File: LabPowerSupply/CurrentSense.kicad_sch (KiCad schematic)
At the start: 7 parts

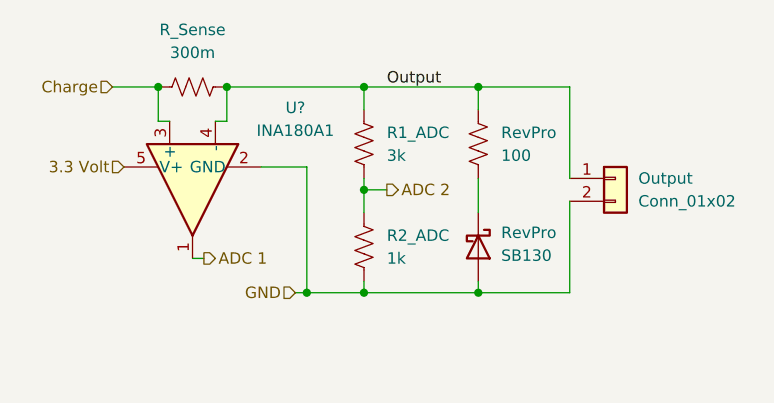
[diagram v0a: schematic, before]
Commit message: Finished first pass on the schematic
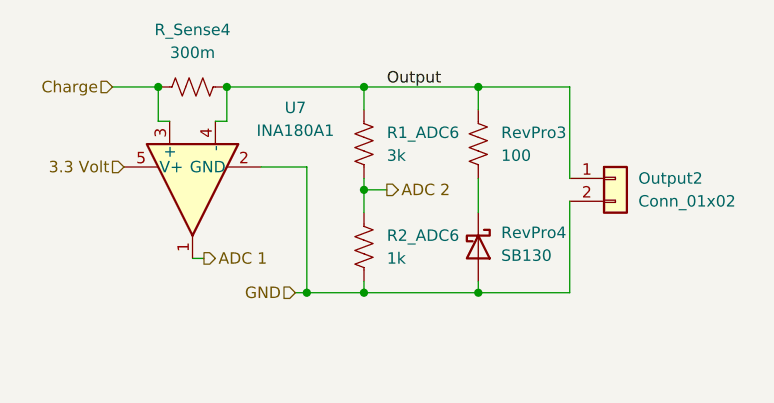
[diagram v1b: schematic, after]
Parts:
- gave numbers to parts that had none: 1
- renumbered Output to Output2, R1_ADC to R1_ADC6, R2_ADC to R2_ADC6, R_Sense to R_Sense4, RevPro to RevPro3, RevPro to RevPro4
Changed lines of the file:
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@@
   (symbol (lib_id "Device:R_US") (at 134.62 83.82 90) (unit 1)
     (in_bom yes) (on_board yes) (fields_autoplaced)
-    (property "Reference" "R_Sense" (id 0) (at 134.62 77.47 90))
+    (property "Reference" "R_Sense4" (id 0) (at 134.62 77.47 90))
     (property "Value" "300m" (id 1) (at 134.62 80.01 90))
     (property "Footprint" "Resistor_SMD:R_1210_3225Metric" (id 2) (at 134.874 82.804 90)
@@
   (symbol (lib_id "Device:R_US") (at 153.67 90.17 0) (unit 1)
     (in_bom yes) (on_board yes) (fields_autoplaced)
-    (property "Reference" "R1_ADC" (id 0) (at 156.21 88.8999 0)
+    (property "Reference" "R1_ADC6" (id 0) (at 156.21 88.8999 0)
       (effects (font (size 1.27 1.27)) (justify left))
     )
@@
   (symbol (lib_id "Device:R_US") (at 166.37 90.17 0) (unit 1)
     (in_bom yes) (on_board yes) (fields_autoplaced)
-    (property "Reference" "RevPro" (id 0) (at 168.91 88.8999 0)
+    (property "Reference" "RevPro3" (id 0) (at 168.91 88.8999 0)
       (effects (font (size 1.27 1.27)) (justify left))
     )
@@
   (symbol (lib_id "Amplifier_Current:INA180A1") (at 134.62 95.25 90) (mirror x) (unit 1)
     (in_bom yes) (on_board yes) (fields_autoplaced)
-    (property "Reference" "U?" (id 0) (at 146.05 86.1312 90))
+    (property "Reference" "U7" (id 0) (at 146.05 86.1312 90))
     (property "Value" "INA180A1" (id 1) (at 146.05 88.6712 90))
     (property "Footprint" "Package_TO_SOT_SMD:SOT-23-5" (id 2) (at 133.35 96.52 0)
@@
   (symbol (lib_id "Connector_Generic:Conn_01x02") (at 181.61 93.98 0) (unit 1)
     (in_bom yes) (on_board yes) (fields_autoplaced)
-    (property "Reference" "Output" (id 0) (at 184.15 93.9799 0)
+    (property "Reference" "Output2" (id 0) (at 184.15 93.9799 0)
       (effects (font (size 1.27 1.27)) (justify left))
     )
@@
   (symbol (lib_id "Diode:SB130") (at 166.37 101.6 270) (unit 1)
     (in_bom yes) (on_board yes) (fields_autoplaced)
-    (property "Reference" "RevPro" (id 0) (at 168.91 100.0124 90)
+    (property "Reference" "RevPro4" (id 0) (at 168.91 100.0124 90)
       (effects (font (size 1.27 1.27)) (justify left))
     )
@@
   (symbol (lib_id "Device:R_US") (at 153.67 101.6 0) (unit 1)
     (in_bom yes) (on_board yes) (fields_autoplaced)
-    (property "Reference" "R2_ADC" (id 0) (at 156.21 100.3299 0)
+    (property "Reference" "R2_ADC6" (id 0) (at 156.21 100.3299 0)
       (effects (font (size 1.27 1.27)) (justify left))
     )

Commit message: started PCB
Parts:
- renumbered U7 to U6
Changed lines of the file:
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@@
   (symbol (lib_id "Amplifier_Current:INA180A1") (at 134.62 95.25 90) (mirror x) (unit 1)
     (in_bom yes) (on_board yes) (fields_autoplaced)
-    (property "Reference" "U7" (id 0) (at 146.05 86.1312 90))
+    (property "Reference" "U6" (id 0) (at 146.05 86.1312 90))
     (property "Value" "INA180A1" (id 1) (at 146.05 88.6712 90))
     (property "Footprint" "Package_TO_SOT_SMD:SOT-23-5" (id 2) (at 133.35 96.52 0)

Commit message: more work
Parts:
- removed RevPro3: 100, Resistor_SMD:R_1210_3225Metric, symbol Device:R_US
- added F_CS1: 320m, Fuse:Fuseholder_Littelfuse_100_series_5x20mm, symbol Device:Fuse
- renumbered U6 to CurrentSense1, RevPro4 to D_CS1, Output2 to Output1, R_Sense4 to R1_CS1, R1_ADC6 to R2_CS1, R2_ADC6 to R3_CS1
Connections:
- net Output: now also D_CS1.1 (K), F_CS1.1; no longer Output1.1 (Pin_1)
- new net: F_CS1.2, Output1.1 (Pin_1)
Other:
- company: (none) -> George Mason University
- title: (none) -> Current and Voltage Sensing
- moved on the sheet: D_CS1
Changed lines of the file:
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@@
 (kicad_sch (version 20211123) (generator eeschema)
   (paper "A4")
+  (title_block
+    (title "Current and Voltage Sensing")
+    (date "2022-09-26")
+    (rev "2")
+    (company "George Mason University")
+    (comment 1 "voltage, and a fuse for reverse polarity protection")
+    (comment 2 "monitered, the voltage senser to both moniter and control the")
+    (comment 3 "user. This stage contains the current senser so that the current can")
+    (comment 4 "This is the final stage before outputting the final voltage for the end")
+  )
   (junction (at 130.81 83.82) (diameter 0) (color 0 0 0 0)
   )
+  (junction (at 153.67 83.82) (diameter 0) (color 0 0 0 0)
+  )
+  (junction (at 153.67 106.68) (diameter 0) (color 0 0 0 0)
+  )
+  (junction (at 153.67 95.25) (diameter 0) (color 0 0 0 0)
+  )
+  (junction (at 147.32 106.68) (diameter 0) (color 0 0 0 0)
+  )
+  (junction (at 138.43 83.82) (diameter 0) (color 0 0 0 0)
+  )
+  (junction (at 166.37 106.68) (diameter 0) (color 0 0 0 0)
+  )
   (junction (at 166.37 83.82) (diameter 0) (color 0 0 0 0)
   )
-  (junction (at 153.67 83.82) (diameter 0) (color 0 0 0 0)
-  )
-  (junction (at 153.67 106.68) (diameter 0) (color 0 0 0 0)
-  )
-  (junction (at 153.67 95.25) (diameter 0) (color 0 0 0 0)
-  )
-  (junction (at 147.32 106.68) (diameter 0) (color 0 0 0 0)
-  )
-  (junction (at 138.43 83.82) (diameter 0) (color 0 0 0 0)
-  )
-  (junction (at 166.37 106.68) (diameter 0) (color 0 0 0 0)
-  )
   (wire (pts (xy 138.43 83.82) (xy 138.43 87.63))
     (stroke (width 0) (type default) (color 0 0 0 0))
@@
     (stroke (width 0) (type default) (color 0 0 0 0))
   )
-  (wire (pts (xy 166.37 93.98) (xy 166.37 97.79))
+  (wire (pts (xy 166.37 83.82) (xy 166.37 91.44))
     (stroke (width 0) (type default) (color 0 0 0 0))
   )
@@
     (stroke (width 0) (type default) (color 0 0 0 0))
   )
+  (wire (pts (xy 175.26 83.82) (xy 176.53 83.82))
+    (stroke (width 0) (type default) (color 0 0 0 0))
+  )
   (wire (pts (xy 153.67 93.98) (xy 153.67 95.25))
     (stroke (width 0) (type default) (color 0 0 0 0))
   )
-  (wire (pts (xy 166.37 83.82) (xy 166.37 86.36))
-    (stroke (width 0) (type default) (color 0 0 0 0))
-  )
   (wire (pts (xy 153.67 95.25) (xy 153.67 97.79))
     (stroke (width 0) (type default) (color 0 0 0 0))
   )
+  (wire (pts (xy 166.37 83.82) (xy 167.64 83.82))
+    (stroke (width 0) (type default) (color 0 0 0 0))
+  )
   (wire (pts (xy 147.32 92.71) (xy 147.32 106.68))
     (stroke (width 0) (type default) (color 0 0 0 0))
@@
     (stroke (width 0) (type default) (color 0 0 0 0))
   )
-  (wire (pts (xy 166.37 105.41) (xy 166.37 106.68))
+  (wire (pts (xy 166.37 99.06) (xy 166.37 106.68))
     (stroke (width 0) (type default) (color 0 0 0 0))
   )
@@
   )
   (wire (pts (xy 146.05 106.68) (xy 147.32 106.68))
-    (stroke (width 0) (type default) (color 0 0 0 0))
-  )
-  (wire (pts (xy 166.37 83.82) (xy 176.53 83.82))
     (stroke (width 0) (type default) (color 0 0 0 0))
   )
@@
     (effects (font (size 1.27 1.27)) (justify right))
   )
+  (symbol (lib_id "Device:Fuse") (at 171.45 83.82 90) (unit 1)
+    (in_bom yes) (on_board yes) (fields_autoplaced)
+    (property "Reference" "F_CS1" (id 0) (at 171.45 77.47 90))
+    (property "Value" "320m" (id 1) (at 171.45 80.01 90))
+    (property "Footprint" "Fuse:Fuseholder_Littelfuse_100_series_5x20mm" (id 2) (at 171.45 85.598 90)
+      (effects (font (size 1.27 1.27)) hide)
+    )
+    (property "Datasheet" "~" (id 3) (at 171.45 83.82 0)
+      (effects (font (size 1.27 1.27)) hide)
+    )
+    (pin "1")
+    (pin "2")
+  )
   (symbol (lib_id "Device:R_US") (at 134.62 83.82 90) (unit 1)
     (in_bom yes) (on_board yes) (fields_autoplaced)
-    (property "Reference" "R_Sense4" (id 0) (at 134.62 77.47 90))
+    (property "Reference" "R1_CS1" (id 0) (at 134.62 77.47 90))
     (property "Value" "300m" (id 1) (at 134.62 80.01 90))
     (property "Footprint" "Resistor_SMD:R_1210_3225Metric" (id 2) (at 134.874 82.804 90)
@@
   (symbol (lib_id "Device:R_US") (at 153.67 90.17 0) (unit 1)
     (in_bom yes) (on_board yes) (fields_autoplaced)
-    (property "Reference" "R1_ADC6" (id 0) (at 156.21 88.8999 0)
+    (property "Reference" "R2_CS1" (id 0) (at 156.21 88.8999 0)
       (effects (font (size 1.27 1.27)) (justify left))
     )
@@
     (pin "2")
   )
-  (symbol (lib_id "Device:R_US") (at 166.37 90.17 0) (unit 1)
-    (in_bom yes) (on_board yes) (fields_autoplaced)
-    (property "Reference" "RevPro3" (id 0) (at 168.91 88.8999 0)
-      (effects (font (size 1.27 1.27)) (justify left))
-    )
-    (property "Value" "100" (id 1) (at 168.91 91.4399 0)
-      (effects (font (size 1.27 1.27)) (justify left))
-    )
-    (property "Footprint" "Resistor_SMD:R_1210_3225Metric" (id 2) (at 167.386 90.424 90)
-      (effects (font (size 1.27 1.27)) hide)
-    )
-    (property "Datasheet" "~" (id 3) (at 166.37 90.17 0)
-      (effects (font (size 1.27 1.27)) hide)
-    )
-    (pin "1")
-    (pin "2")
-  )
   (symbol (lib_id "Amplifier_Current:INA180A1") (at 134.62 95.25 90) (mirror x) (unit 1)
-    (in_bom yes) (on_board yes) (fields_autoplaced)
-    (property "Reference" "U6" (id 0) (at 146.05 86.1312 90))
-    (property "Value" "INA180A1" (id 1) (at 146.05 88.6712 90))
+    (in_bom yes) (on_board yes)
+    (property "Reference" "CurrentSense1" (id 0) (at 124.46 97.79 90))
+    (property "Value" "INA180A1" (id 1) (at 124.46 100.33 90))
     (property "Footprint" "Package_TO_SOT_SMD:SOT-23-5" (id 2) (at 133.35 96.52 0)
       (effects (font (size 1.27 1.27)) hide)
@@
   (symbol (lib_id "Connector_Generic:Conn_01x02") (at 181.61 93.98 0) (unit 1)
     (in_bom yes) (on_board yes) (fields_autoplaced)
-    (property "Reference" "Output2" (id 0) (at 184.15 93.9799 0)
+    (property "Reference" "Output1" (id 0) (at 184.15 93.9799 0)
       (effects (font (size 1.27 1.27)) (justify left))
     )
@@
     (pin "2")
   )
-  (symbol (lib_id "Diode:SB130") (at 166.37 101.6 270) (unit 1)
-    (in_bom yes) (on_board yes) (fields_autoplaced)
-    (property "Reference" "RevPro4" (id 0) (at 168.91 100.0124 90)
-      (effects (font (size 1.27 1.27)) (justify left))
-    )
-    (property "Value" "SB130" (id 1) (at 168.91 102.5524 90)
-      (effects (font (size 1.27 1.27)) (justify left))
-    )
-    (property "Footprint" "Diode_THT:D_DO-41_SOD81_P10.16mm_Horizontal" (id 2) (at 161.925 101.6 0)
-      (effects (font (size 1.27 1.27)) hide)
-    )
-    (property "Datasheet" "http://www.diodes.com/_files/datasheets/ds23022.pdf" (id 3) (at 166.37 101.6 0)
+  (symbol (lib_id "Diode:SB130") (at 166.37 95.25 270) (unit 1)
+    (in_bom yes) (on_board yes) (fields_autoplaced)
+    (property "Reference" "D_CS1" (id 0) (at 168.91 93.6624 90)
+      (effects (font (size 1.27 1.27)) (justify left))
+    )
+    (property "Value" "SB130" (id 1) (at 168.91 96.2024 90)
+      (effects (font (size 1.27 1.27)) (justify left))
+    )
+    (property "Footprint" "Diode_THT:D_DO-41_SOD81_P10.16mm_Horizontal" (id 2) (at 161.925 95.25 0)
+      (effects (font (size 1.27 1.27)) hide)
+    )
+    (property "Datasheet" "http://www.diodes.com/_files/datasheets/ds23022.pdf" (id 3) (at 166.37 95.25 0)
       (effects (font (size 1.27 1.27)) hide)
     )
@@
   (symbol (lib_id "Device:R_US") (at 153.67 101.6 0) (unit 1)
     (in_bom yes) (on_board yes) (fields_autoplaced)
-    (property "Reference" "R2_ADC6" (id 0) (at 156.21 100.3299 0)
-      (effects (font (size 1.27 1.27)) (justify left))
-    )
+    (property "Reference" "R3_CS1" (id 0) (at 156.21 100.3299 0)
+      (effects (font (size 1.27 1.27)) (justify left))
+    )

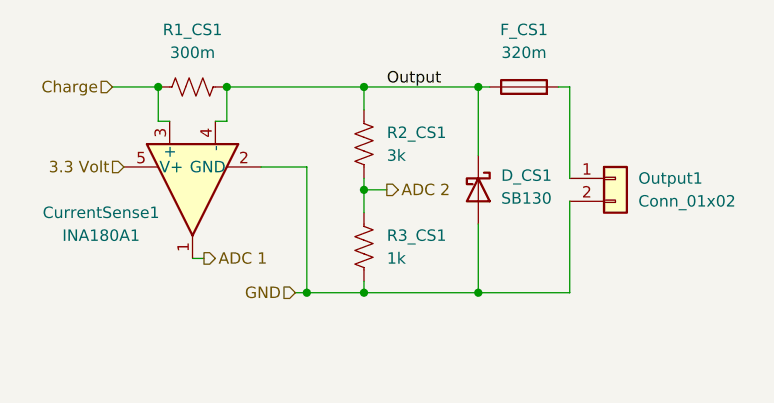
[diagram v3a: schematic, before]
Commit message: Resistor footprints changed to 0603
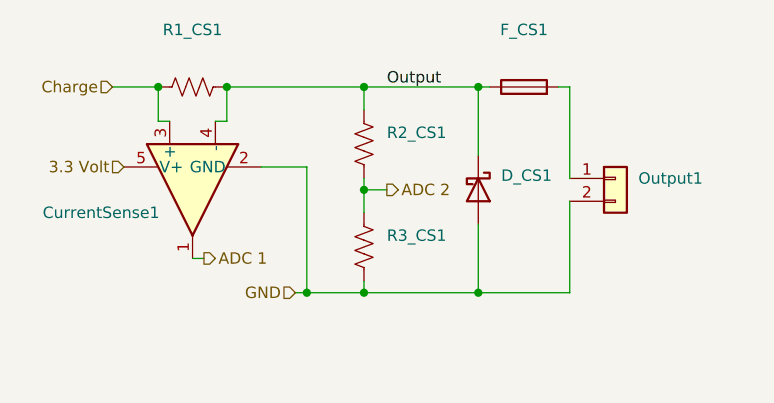
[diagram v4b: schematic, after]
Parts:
- CurrentSense1: value INA180A1 -> (none); footprint Package_TO_SOT_SMD:SOT-23-5 -> (none)
- D_CS1: value SB130 -> (none); footprint Diode_THT:D_DO-41_SOD81_P10.16mm_Horizontal -> (none)
- F_CS1: value 320m -> (none); footprint Fuse:Fuseholder_Littelfuse_100_series_5x20mm -> (none)
- Output1: value Conn_01x02 -> (none); footprint Connector_Wire:SolderWire-2sqmm_1x02_P7.8mm_D2mm_OD3.9mm -> (none)
- R1_CS1: value 300m -> (none); footprint Resistor_SMD:R_1210_3225Metric -> (none)
- R2_CS1: value 3k -> (none); footprint Resistor_SMD:R_1210_3225Metric -> (none)
- R3_CS1: value 1k -> (none); footprint Resistor_SMD:R_1210_3225Metric -> (none)
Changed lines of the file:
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@@
     (in_bom yes) (on_board yes) (fields_autoplaced)
     (property "Reference" "F_CS1" (id 0) (at 171.45 77.47 90))
-    (property "Value" "320m" (id 1) (at 171.45 80.01 90))
-    (property "Footprint" "Fuse:Fuseholder_Littelfuse_100_series_5x20mm" (id 2) (at 171.45 85.598 90)
+    (property "Value" "" (id 1) (at 171.45 80.01 90))
+    (property "Footprint" "" (id 2) (at 171.45 85.598 90)
       (effects (font (size 1.27 1.27)) hide)
     )
@@
     (in_bom yes) (on_board yes) (fields_autoplaced)
     (property "Reference" "R1_CS1" (id 0) (at 134.62 77.47 90))
-    (property "Value" "300m" (id 1) (at 134.62 80.01 90))
-    (property "Footprint" "Resistor_SMD:R_1210_3225Metric" (id 2) (at 134.874 82.804 90)
+    (property "Value" "" (id 1) (at 134.62 80.01 90))
+    (property "Footprint" "" (id 2) (at 134.874 82.804 90)
       (effects (font (size 1.27 1.27)) hide)
     )
@@
       (effects (font (size 1.27 1.27)) (justify left))
     )
-    (property "Value" "3k" (id 1) (at 156.21 91.4399 0)
+    (property "Value" "" (id 1) (at 156.21 91.4399 0)
       (effects (font (size 1.27 1.27)) (justify left))
     )
-    (property "Footprint" "Resistor_SMD:R_1210_3225Metric" (id 2) (at 154.686 90.424 90)
+    (property "Footprint" "" (id 2) (at 154.686 90.424 90)
       (effects (font (size 1.27 1.27)) hide)
     )
@@
     (in_bom yes) (on_board yes)
     (property "Reference" "CurrentSense1" (id 0) (at 124.46 97.79 90))
-    (property "Value" "INA180A1" (id 1) (at 124.46 100.33 90))
-    (property "Footprint" "Package_TO_SOT_SMD:SOT-23-5" (id 2) (at 133.35 96.52 0)
+    (property "Value" "" (id 1) (at 124.46 100.33 90))
+    (property "Footprint" "" (id 2) (at 133.35 96.52 0)
       (effects (font (size 1.27 1.27)) hide)
     )
@@
       (effects (font (size 1.27 1.27)) (justify left))
     )
-    (property "Value" "Conn_01x02" (id 1) (at 184.15 96.5199 0)
+    (property "Value" "" (id 1) (at 184.15 96.5199 0)
       (effects (font (size 1.27 1.27)) (justify left))
     )
-    (property "Footprint" "Connector_Wire:SolderWire-2sqmm_1x02_P7.8mm_D2mm_OD3.9mm" (id 2) (at 181.61 93.98 0)
+    (property "Footprint" "" (id 2) (at 181.61 93.98 0)
       (effects (font (size 1.27 1.27)) hide)
     )
@@
       (effects (font (size 1.27 1.27)) (justify left))
     )
-    (property "Value" "SB130" (id 1) (at 168.91 96.2024 90)
+    (property "Value" "" (id 1) (at 168.91 96.2024 90)
       (effects (font (size 1.27 1.27)) (justify left))
     )
-    (property "Footprint" "Diode_THT:D_DO-41_SOD81_P10.16mm_Horizontal" (id 2) (at 161.925 95.25 0)
+    (property "Footprint" "" (id 2) (at 161.925 95.25 0)
       (effects (font (size 1.27 1.27)) hide)
     )
@@
       (effects (font (size 1.27 1.27)) (justify left))
     )
-    (property "Value" "1k" (id 1) (at 156.21 102.8699 0)
+    (property "Value" "" (id 1) (at 156.21 102.8699 0)
       (effects (font (size 1.27 1.27)) (justify left))
     )
-    (property "Footprint" "Resistor_SMD:R_1210_3225Metric" (id 2) (at 154.686 101.854 90)
+    (property "Footprint" "" (id 2) (at 154.686 101.854 90)
       (effects (font (size 1.27 1.27)) hide)
     )

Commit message: Added mcu capacitors, split 5v inductors
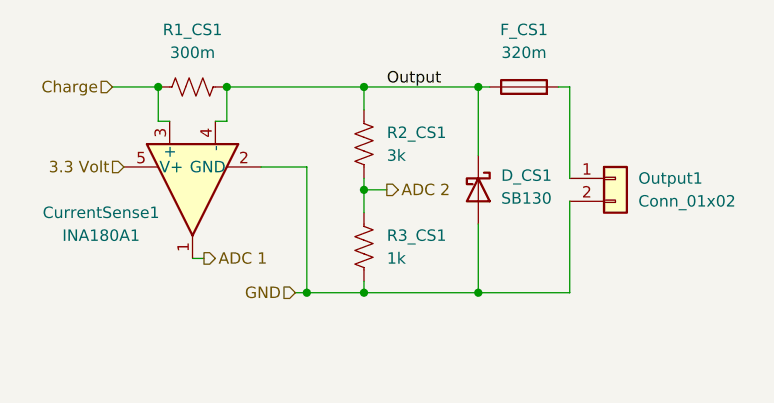
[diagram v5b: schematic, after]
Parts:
- CurrentSense1: value (none) -> INA180A1; footprint (none) -> Package_TO_SOT_SMD:SOT-23-5
- D_CS1: value (none) -> SB130; footprint (none) -> Diode_THT:D_DO-41_SOD81_P10.16mm_Horizontal
- F_CS1: value (none) -> 320m; footprint (none) -> Fuse:Fuseholder_Littelfuse_100_series_5x20mm
- Output1: value (none) -> Conn_01x02; footprint (none) -> Connector_Wire:SolderWire-2sqmm_1x02_P7.8mm_D2mm_OD3.9mm
- R1_CS1: value (none) -> 300m; footprint (none) -> Resistor_SMD:R_0603_1608Metric
- R2_CS1: value (none) -> 3k; footprint (none) -> Resistor_SMD:R_0603_1608Metric
- R3_CS1: value (none) -> 1k; footprint (none) -> Resistor_SMD:R_0603_1608Metric
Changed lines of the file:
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@@
     (in_bom yes) (on_board yes) (fields_autoplaced)
     (property "Reference" "F_CS1" (id 0) (at 171.45 77.47 90))
-    (property "Value" "" (id 1) (at 171.45 80.01 90))
-    (property "Footprint" "" (id 2) (at 171.45 85.598 90)
+    (property "Value" "320m" (id 1) (at 171.45 80.01 90))
+    (property "Footprint" "Fuse:Fuseholder_Littelfuse_100_series_5x20mm" (id 2) (at 171.45 85.598 90)
       (effects (font (size 1.27 1.27)) hide)
     )
@@
     (in_bom yes) (on_board yes) (fields_autoplaced)
     (property "Reference" "R1_CS1" (id 0) (at 134.62 77.47 90))
-    (property "Value" "" (id 1) (at 134.62 80.01 90))
-    (property "Footprint" "" (id 2) (at 134.874 82.804 90)
+    (property "Value" "300m" (id 1) (at 134.62 80.01 90))
+    (property "Footprint" "Resistor_SMD:R_0603_1608Metric" (id 2) (at 134.874 82.804 90)
       (effects (font (size 1.27 1.27)) hide)
     )
@@
       (effects (font (size 1.27 1.27)) (justify left))
     )
-    (property "Value" "" (id 1) (at 156.21 91.4399 0)
+    (property "Value" "3k" (id 1) (at 156.21 91.4399 0)
       (effects (font (size 1.27 1.27)) (justify left))
     )
-    (property "Footprint" "" (id 2) (at 154.686 90.424 90)
+    (property "Footprint" "Resistor_SMD:R_0603_1608Metric" (id 2) (at 154.686 90.424 90)
       (effects (font (size 1.27 1.27)) hide)
     )
@@
     (in_bom yes) (on_board yes)
     (property "Reference" "CurrentSense1" (id 0) (at 124.46 97.79 90))
-    (property "Value" "" (id 1) (at 124.46 100.33 90))
-    (property "Footprint" "" (id 2) (at 133.35 96.52 0)
+    (property "Value" "INA180A1" (id 1) (at 124.46 100.33 90))
+    (property "Footprint" "Package_TO_SOT_SMD:SOT-23-5" (id 2) (at 133.35 96.52 0)
       (effects (font (size 1.27 1.27)) hide)
     )
@@
       (effects (font (size 1.27 1.27)) (justify left))
     )
-    (property "Value" "" (id 1) (at 184.15 96.5199 0)
+    (property "Value" "Conn_01x02" (id 1) (at 184.15 96.5199 0)
       (effects (font (size 1.27 1.27)) (justify left))
     )
-    (property "Footprint" "" (id 2) (at 181.61 93.98 0)
+    (property "Footprint" "Connector_Wire:SolderWire-2sqmm_1x02_P7.8mm_D2mm_OD3.9mm" (id 2) (at 181.61 93.98 0)
       (effects (font (size 1.27 1.27)) hide)
     )
@@
       (effects (font (size 1.27 1.27)) (justify left))
     )
-    (property "Value" "" (id 1) (at 168.91 96.2024 90)
+    (property "Value" "SB130" (id 1) (at 168.91 96.2024 90)
       (effects (font (size 1.27 1.27)) (justify left))
     )
-    (property "Footprint" "" (id 2) (at 161.925 95.25 0)
+    (property "Footprint" "Diode_THT:D_DO-41_SOD81_P10.16mm_Horizontal" (id 2) (at 161.925 95.25 0)
       (effects (font (size 1.27 1.27)) hide)
     )
@@
       (effects (font (size 1.27 1.27)) (justify left))
     )
-    (property "Value" "" (id 1) (at 156.21 102.8699 0)
+    (property "Value" "1k" (id 1) (at 156.21 102.8699 0)
       (effects (font (size 1.27 1.27)) (justify left))
     )
-    (property "Footprint" "" (id 2) (at 154.686 101.854 90)
+    (property "Footprint" "Resistor_SMD:R_0603_1608Metric" (id 2) (at 154.686 101.854 90)
       (effects (font (size 1.27 1.27)) hide)
     )
